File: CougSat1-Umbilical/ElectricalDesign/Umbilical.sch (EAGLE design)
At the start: 47 parts, among them J1 USB, J2 Umbilical, J3 5V input, Q1 CSD16406Q3, Q2 CSD16406Q3, U1 FT230XQ, U2 BQ24650

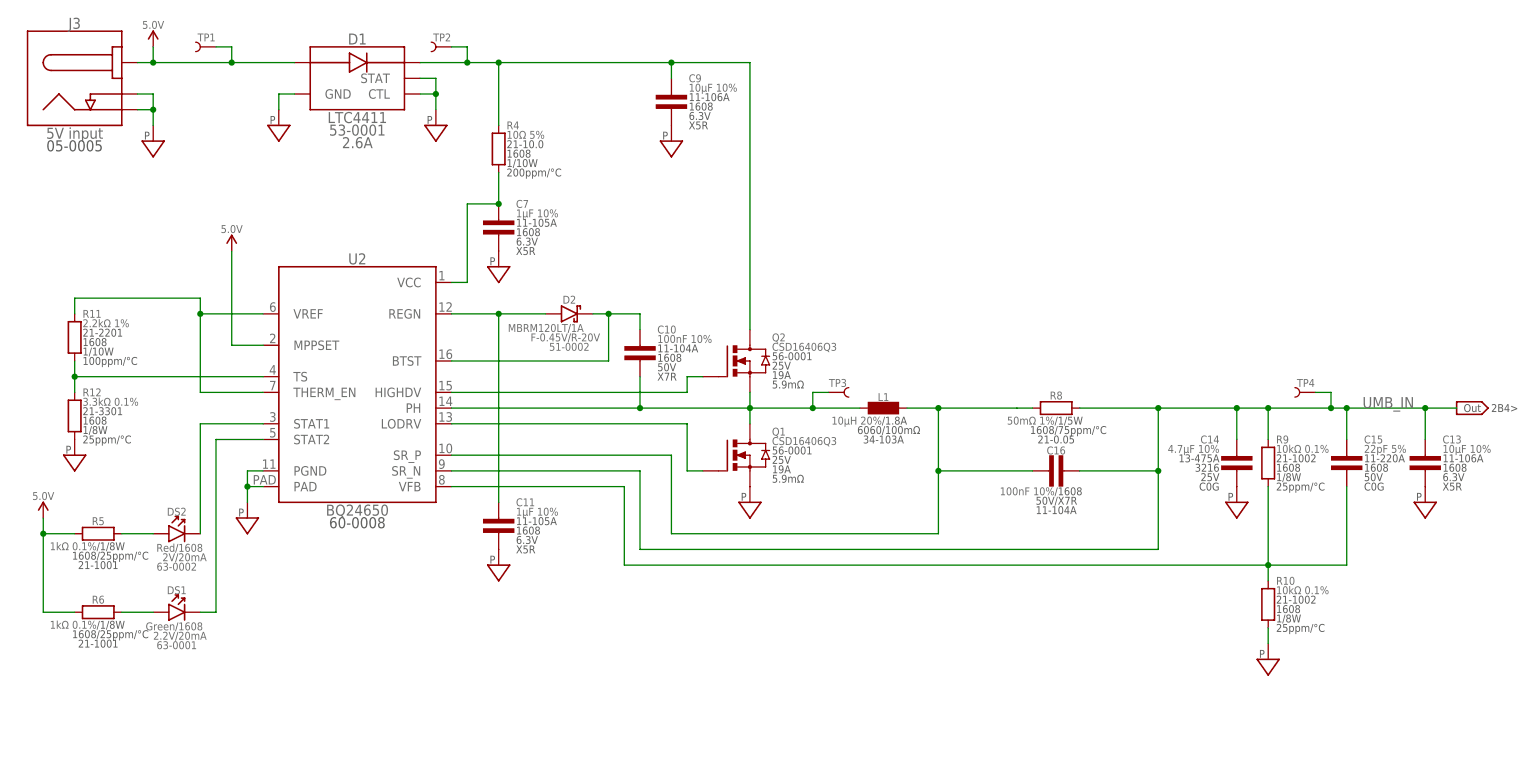
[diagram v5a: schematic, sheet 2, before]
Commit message: Fixed formatting
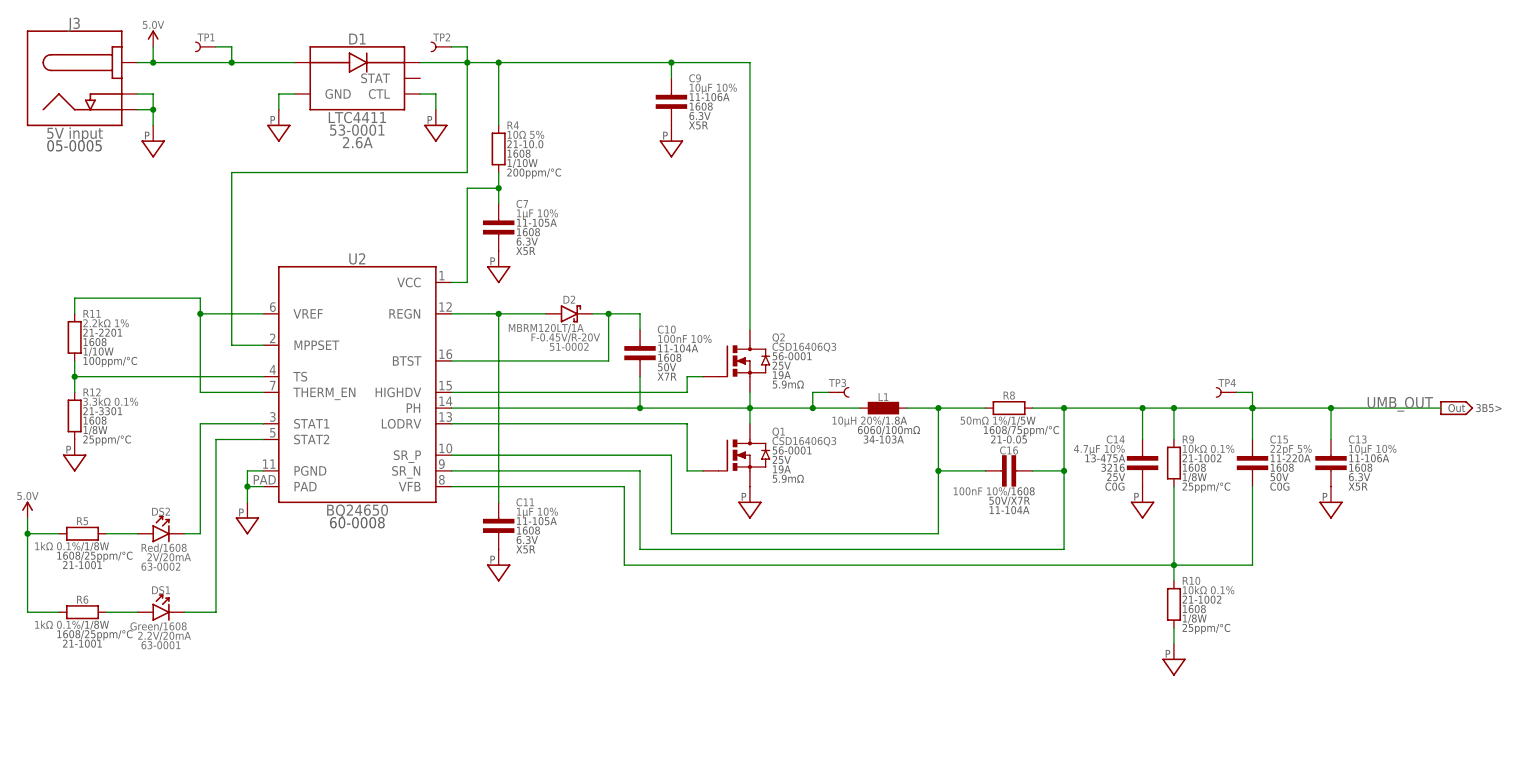
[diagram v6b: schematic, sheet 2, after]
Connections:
- net UMB_IN renamed UMB_OUT
- net 5.0V: no longer U2.MPPSET
- net DIODE_OUT: now also U2.MPPSET
- net PGND: no longer D1.STAT
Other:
- note added: "2B6>"
- note added: "3B5>"
- note removed: "2B4>"
- note removed: "3B6>"
- moved on the sheet: C1, C13, C14, C15, C16, DS1, DS2, J2, R10, R5, R6, R8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

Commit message: Merged and fixed conflicts
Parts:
- added DS3: Green, CougsInSpace-LEDs:LED-V-GRN-1608
- added DS5: Red, CougsInSpace-LEDs:LED-V-RED-1608
- added R13, R15: 1kΩ 0.1%, CougsInSpace-Resistors:RES-H-1K-1608
- added RN1: 10kΩ 1%, CougsInSpace-Resistors:RES-4-V-10K-1632
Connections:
- new net !CTS: RN1D.1, U1.!CTS
- new net !RTS: RN1C.1, U1.!RTS
- new net CBUS1: R15.1, U1.CBUS1
- new net CBUS2: R13.1, U1.CBUS2
- new net RXLED_C: DS5.C, R13.2
- new net TXLED_C: DS3.C, R15.2
- net 3.3V: now also DS3.A, DS5.A, RN1A.2, RN1B.2, RN1C.2, RN1D.2
- net UMB_RX: now also RN1A.1
- net UMB_TX: now also RN1B.1
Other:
- moved on the sheet: J2

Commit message: Updated Umbilical
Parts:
- added R16, R17: 0Ω <20mΩ, CougsInSpace-Resistors:RES-V-0-1608
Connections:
- new net N$1: R16.2, R9.1
- new net N$2: R10.2, R17.1
- net !CTS: now also U1.CTS; no longer U1.!CTS
- net !RTS: now also U1.RTS; no longer U1.!RTS
- net VFB: now also R16.1, R17.2; no longer R10.2, R9.1
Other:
- moved on the sheet: R10
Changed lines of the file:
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@@
 <?xml version="1.0" encoding="utf-8"?>
 <!DOCTYPE eagle SYSTEM "eagle.dtd">
-<eagle version="9.4.2">
+<eagle version="9.3.2">
 <drawing>
 <settings>
@@
 <setting verticaltext="up"/>
 </settings>
-<grid distance="0.1" unitdist="inch" unit="inch" style="lines" multiple="1" display="no" altdistance="0.05" altunitdist="inch" altunit="inch"/>
+<grid distance="0.1" unitdist="inch" unit="inch" style="lines" multiple="1" display="no" altdistance="0.01" altunitdist="inch" altunit="inch"/>
 <layers>
 <layer number="1" name="Top" color="4" fill="1" visible="no" active="no"/>
@@
 <part name="RN1" library="CougsInSpace-Resistors" deviceset="RES-4-V" device="-1632" technology="-10K" value="10kΩ 1%"/>
 <part name="SUPPLY31" library="CougsInSpace-PowerSymbols" deviceset="3.3V" device=""/>
+<part name="R16" library="CougsInSpace-Resistors" deviceset="RES-V" device="-1608" technology="-0" value="0Ω &lt;20mΩ"/>
+<part name="R17" library="CougsInSpace-Resistors" deviceset="RES-V" device="-1608" technology="-0" value="0Ω &lt;20mΩ"/>
 </parts>
 <sheets>
@@
 <attribute name="SKU" x="199.39" y="103.632" size="1.27" layer="97" align="center-left"/>
 </instance>
-<instance part="SUPPLY25" gate="G$1" x="198.12" y="71.12" smashed="yes"/>
+<instance part="SUPPLY25" gate="G$1" x="198.12" y="58.42" smashed="yes"/>
 <instance part="R11" gate="G$1" x="20.32" y="121.92" smashed="yes">
 <attribute name="NAME" x="21.59" y="127" size="1.27" layer="95" align="center-left"/>
@@
 <attribute name="SKU" x="21.59" y="73.66" size="1.27" layer="97" align="center"/>
 </instance>
-<instance part="R10" gate="G$1" x="198.12" y="78.74" smashed="yes">
-<attribute name="NAME" x="199.39" y="83.82" size="1.27" layer="95" align="center-left"/>
-<attribute name="VALUE" x="199.39" y="82.296" size="1.27" layer="96" align="center-left"/>
-<attribute name="PACKAGE" x="199.39" y="79.248" size="1.27" layer="97" align="center-left"/>
-<attribute name="POWER" x="199.39" y="77.724" size="1.27" layer="97" align="center-left"/>
-<attribute name="TEMP" x="199.39" y="76.2" size="1.27" layer="97" align="center-left"/>
-<attribute name="SKU" x="199.39" y="80.772" size="1.27" layer="97" align="center-left"/>
+<instance part="R10" gate="G$1" x="198.12" y="66.04" smashed="yes">
+<attribute name="NAME" x="199.39" y="71.12" size="1.27" layer="95" align="center-left"/>
+<attribute name="VALUE" x="199.39" y="69.596" size="1.27" layer="96" align="center-left"/>
+<attribute name="PACKAGE" x="199.39" y="66.548" size="1.27" layer="97" align="center-left"/>
+<attribute name="POWER" x="199.39" y="65.024" size="1.27" layer="97" align="center-left"/>
+<attribute name="TEMP" x="199.39" y="63.5" size="1.27" layer="97" align="center-left"/>
+<attribute name="SKU" x="199.39" y="68.072" size="1.27" layer="97" align="center-left"/>
 </instance>
 <instance part="R8" gate="G$1" x="172.72" y="111.76" smashed="yes">
@@
 </instance>
 <instance part="OFFSHEET2" gate="G$1" x="243.84" y="111.76" smashed="yes" rot="MR0"/>
+<instance part="R16" gate="G$1" x="198.12" y="91.44" smashed="yes">
+<attribute name="NAME" x="199.39" y="96.52" size="1.27" layer="95" align="center-left"/>
+<attribute name="VALUE" x="199.39" y="94.996" size="1.27" layer="96" align="center-left"/>
+<attribute name="PACKAGE" x="199.39" y="91.948" size="1.27" layer="97" align="center-left"/>
+<attribute name="POWER" x="199.39" y="90.424" size="1.27" layer="97" align="center-left"/>
+<attribute name="TEMP" x="199.39" y="88.9" size="1.27" layer="97" align="center-left"/>
+<attribute name="SKU" x="199.39" y="93.472" size="1.27" layer="97" align="center-left"/>
+</instance>
+<instance part="R17" gate="G$1" x="198.12" y="78.74" smashed="yes">
+<attribute name="NAME" x="199.39" y="83.82" size="1.27" layer="95" align="center-left"/>
+<attribute name="VALUE" x="199.39" y="82.296" size="1.27" layer="96" align="center-left"/>
+<attribute name="PACKAGE" x="199.39" y="79.248" size="1.27" layer="97" align="center-left"/>
+<attribute name="POWER" x="199.39" y="77.724" size="1.27" layer="97" align="center-left"/>
+<attribute name="TEMP" x="199.39" y="76.2" size="1.27" layer="97" align="center-left"/>
+<attribute name="SKU" x="199.39" y="80.772" size="1.27" layer="97" align="center-left"/>
+</instance>
 </instances>
 <busses>
@@
 <segment>
 <pinref part="SUPPLY25" gate="G$1" pin="PGND"/>
-<wire x1="198.12" y1="73.66" x2="198.12" y2="76.2" width="0.1524" layer="91"/>
+<wire x1="198.12" y1="60.96" x2="198.12" y2="63.5" width="0.1524" layer="91"/>
 <pinref part="R10" gate="G$1" pin="1"/>
 </segment>
@@
 <wire x1="210.82" y1="99.06" x2="210.82" y2="86.36" width="0.1524" layer="91"/>
 <wire x1="210.82" y1="86.36" x2="198.12" y2="86.36" width="0.1524" layer="91"/>
-<pinref part="R9" gate="G$1" pin="1"/>
 <wire x1="198.12" y1="86.36" x2="109.22" y2="86.36" width="0.1524" layer="91"/>
+<junction x="198.12" y="86.36"/>
+<wire x1="198.12" y1="86.36" x2="198.12" y2="88.9" width="0.1524" layer="91"/>
+<pinref part="R16" gate="G$1" pin="1"/>
 <wire x1="198.12" y1="83.82" x2="198.12" y2="86.36" width="0.1524" layer="91"/>
-<junction x="198.12" y="86.36"/>
-<wire x1="198.12" y1="86.36" x2="198.12" y2="99.06" width="0.1524" layer="91"/>
-<pinref part="R10" gate="G$1" pin="2"/>
+<pinref part="R17" gate="G$1" pin="2"/>
 </segment>
 </net>
@@
 <wire x1="50.8" y1="116.84" x2="20.32" y2="116.84" width="0.1524" layer="91"/>
 <junction x="20.32" y="116.84"/>
+</segment>
+</net>
+<net name="N$1" class="0">
+<segment>
+<pinref part="R9" gate="G$1" pin="1"/>
+<wire x1="198.12" y1="96.52" x2="198.12" y2="99.06" width="0.1524" layer="91"/>
+<pinref part="R16" gate="G$1" pin="2"/>
+</segment>
+</net>
+<net name="N$2" class="0">
+<segment>
+<pinref part="R17" gate="G$1" pin="1"/>
+<pinref part="R10" gate="G$1" pin="2"/>
+<wire x1="198.12" y1="76.2" x2="198.12" y2="71.12" width="0.1524" layer="91"/>
 </segment>
 </net>
@@
 <segment>
 <pinref part="RN1" gate="D" pin="1"/>
-<pinref part="U1" gate="G$1" pin="!CTS"/>
+<pinref part="U1" gate="G$1" pin="CTS"/>
 <wire x1="193.04" y1="147.32" x2="193.04" y2="119.38" width="0.1524" layer="91"/>
 <wire x1="193.04" y1="119.38" x2="162.56" y2="119.38" width="0.1524" layer="91"/>
@@
 <net name="!RTS" class="0">
 <segment>
-<pinref part="U1" gate="G$1" pin="!RTS"/>
+<pinref part="U1" gate="G$1" pin="RTS"/>
 <pinref part="RN1" gate="C" pin="1"/>
 <wire x1="162.56" y1="121.92" x2="180.34" y2="121.92" width="0.1524" layer="91"/>
